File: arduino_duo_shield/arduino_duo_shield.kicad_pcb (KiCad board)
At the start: 2 copper layers, 102.1 x 119.4 mm, 76 parts, among them J2 EStop, J3 Motor_Control, J4 Limit_Switches, J5 inverter_freq, J6 inverter_cmd, J8 inverter_power, J9 Motor_Control_Mirror, K2 JQC-3F, K3 JQC-3F, P10 Digital, P11 PWM, P12 PWM, P13 Communication, P7 Power, P8 Analog, P9 Analog, Q3 2N7000, Q4 BS250, Q5 2N7000, Q6 2N7000, SW1 SW_Push, U1 4504, U2 4504, U3 LM358, U4 74HC14, U6 74HC14, U7 PC817, U8 PC817, U9 PC817

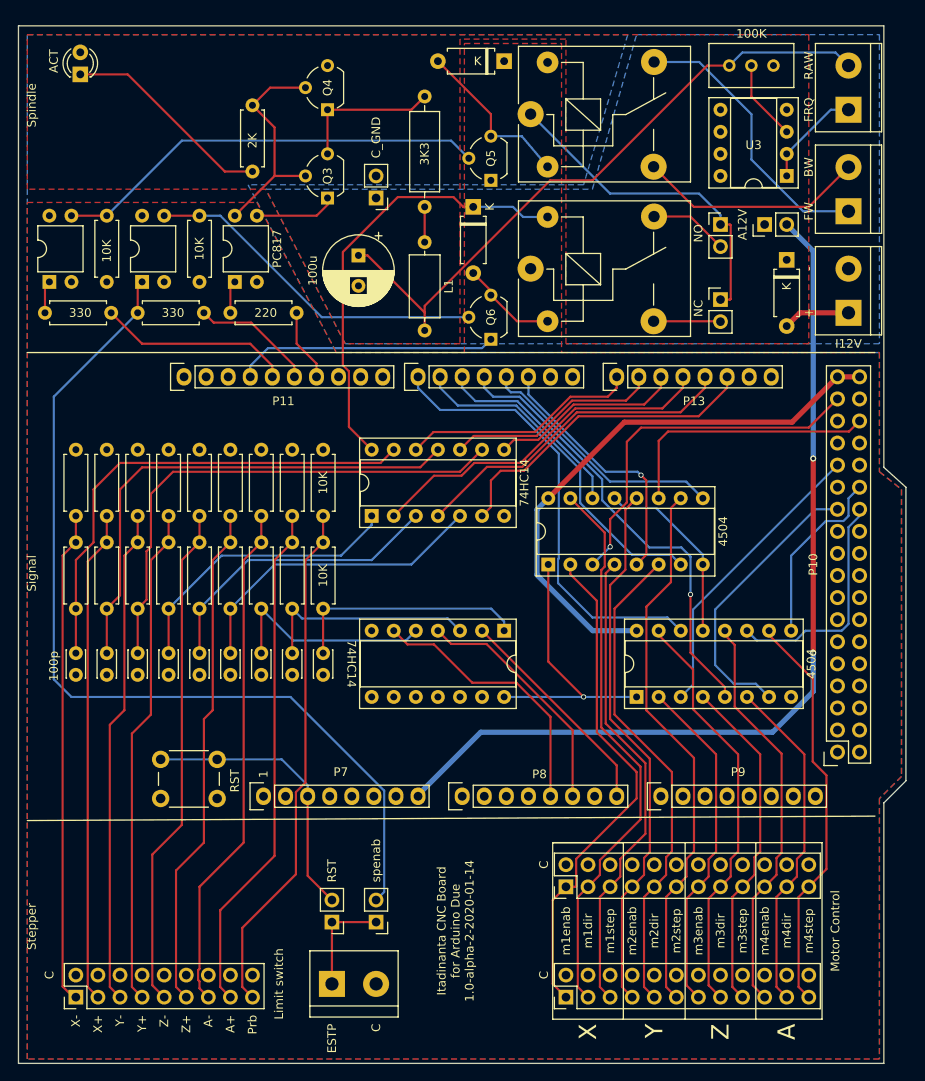
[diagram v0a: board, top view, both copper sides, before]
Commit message: Added screw connectors to everything
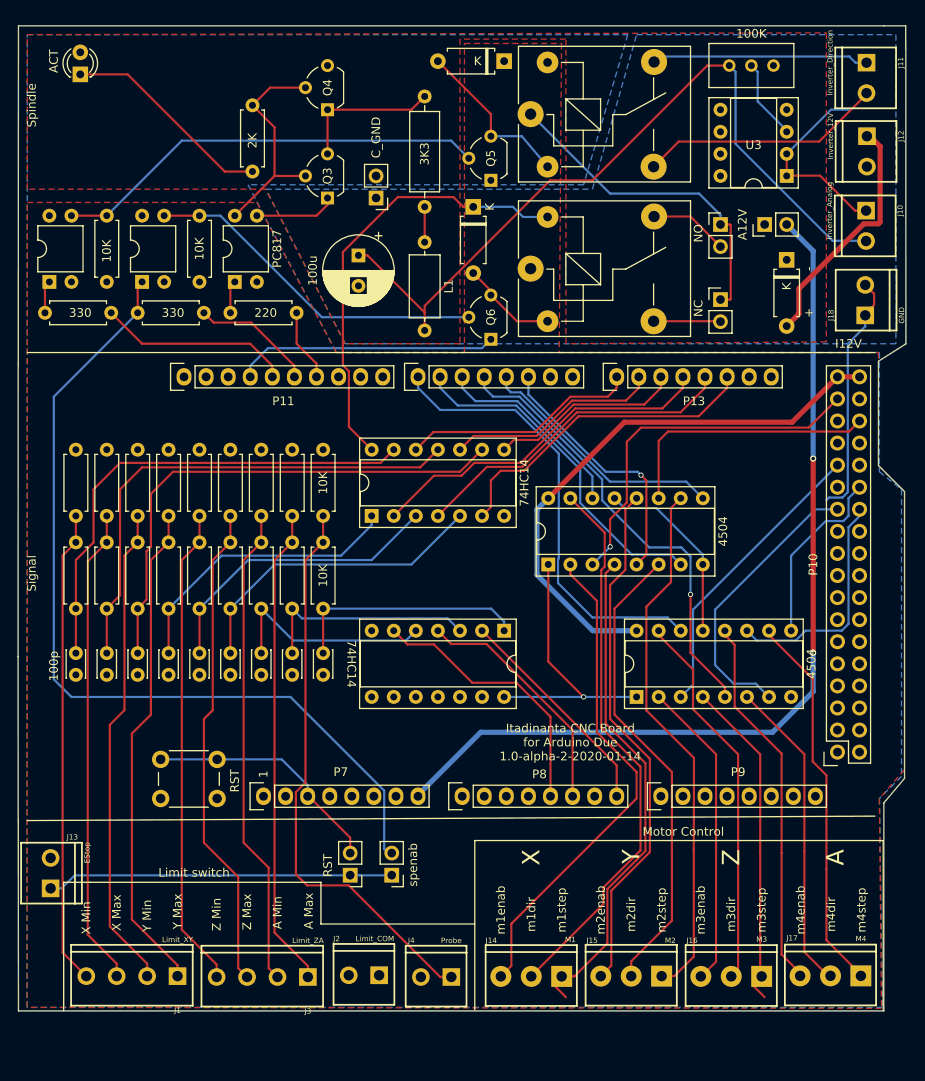
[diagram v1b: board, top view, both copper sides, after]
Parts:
- removed J5: inverter_freq, TerminalBlock:TerminalBlock_bornier-2_P5.08mm
- removed J6: inverter_cmd, TerminalBlock:TerminalBlock_bornier-2_P5.08mm
- removed J8: inverter_power, TerminalBlock:TerminalBlock_bornier-2_P5.08mm
- removed J9: Motor_Control_Mirror, Connector_PinHeader_2.54mm:PinHeader_2x12_P2.54mm_Vertical
- added J1: Limit_XY, Connectors:SCREWTERMINAL-3.5MM-4, F.Cu at (121.4, 139.8)
- added J10: Inverter_Analog, Connectors:SCREWTERMINAL-3.5MM-2, F.Cu at (200.6, 51.7)
- added J11: Inverter_Direction, Connectors:SCREWTERMINAL-3.5MM-2, F.Cu at (200.7, 34.7)
- added J12: Inverter_12V, Connectors:SCREWTERMINAL-3.5MM-2, F.Cu at (200.7, 43.2)
- added J13: EStop, Connectors:SCREWTERMINAL-3.5MM-2, F.Cu at (106.8, 129.7)
- added J14: M1, Connectors:SCREWTERMINAL-3.5MM-3, F.Cu at (165.6, 139.8)
- added J15: M2, Connectors:SCREWTERMINAL-3.5MM-3, F.Cu at (177.1, 139.8)
- added J16: M3, Connectors:SCREWTERMINAL-3.5MM-3, F.Cu at (188.6, 139.8)
- added J17: M4, Connectors:SCREWTERMINAL-3.5MM-3, F.Cu at (200.1, 139.8)
- added J18: GND, Connectors:SCREWTERMINAL-3.5MM-2, F.Cu at (200.6, 63.8)
- J2: value EStop -> Limit_COM; footprint TerminalBlock:TerminalBlock_bornier-2_P5.08mm -> Connectors:SCREWTERMINAL-3.5MM-2
- J3: value Motor_Control -> Limit_ZA; footprint Connector_PinHeader_2.54mm:PinHeader_2x12_P2.54mm_Vertical -> Connectors:SCREWTERMINAL-3.5MM-4
- J4: value Limit_Switches -> Probe; footprint Connector_PinHeader_2.54mm:PinHeader_2x09_P2.54mm_Vertical -> Connectors:SCREWTERMINAL-3.5MM-2
- moved J4 43.3 mm to (152.9, 139.9), turned to 180 degrees
- moved J3 31.5 mm to (136.4, 139.9), turned to 180 degrees
- moved JP5 5.79 mm to (141.3, 128.2)
- moved JP6 5.69 mm to (146.1, 128.2)
- moved J2 5.52 mm to (144.6, 139.7), turned to 180 degrees
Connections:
- J2 pad 1: Net-(J2-Pad1) -> GND
- J3 pad 1: /Level_Shifter/hi_1_1 -> /Debounce_x6/SWAmax+
- J3 pad 2: GND -> /Debounce_x6/SWAmin+
- J3 pad 3: /Level_Shifter/hi_1_2 -> /Debounce_x6/SWZmax+
- J3 pad 4: GND -> /Debounce_x6/SWZmin+
- J4 pad 1: /Debounce_x6/SWXmin+ -> /Debounce_x6/SWProbe+
- JP5 pad 1: Net-(J2-Pad1) -> Net-(J13-Pad1)
- JP6 pad 1: Net-(J2-Pad1) -> Net-(J13-Pad1)
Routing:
- net Net-(J13-Pad1): track 0.00 -> 40.0 mm
- net GND: track 51.8 -> 80.7 mm
- net /Spindle_VFD_Control/inverter_12V: track 7.74 -> 28.0 mm
- net /Spindle_VFD_Control/inverter_frequency_raw_10V: track 74.6 -> 88.8 mm
- net Net-(J2-Pad1): track 12.2 -> 0.00 mm
- net /Spindle_VFD_Control/inverter_frequency_10V: track 11.8 -> 22.4 mm
- net /Spindle_VFD_Control/inverter_fw_switch: track 32.6 -> 26.2 mm
- net /Debounce_x6/SWProbe+: track 59.7 -> 65.3 mm
- net /Spindle_VFD_Control/ext_estop: track 106.2 -> 101.2 mm
- net /Reset: track 32.5 -> 28.1 mm
- net /Level_Shifter/hi_2_2: track 47.9 -> 43.9 mm
- net /Debounce_x6/SWAmax+: track 59.3 -> 55.5 mm
- net /Level_Shifter/hi_2_1: track 39.3 -> 35.7 mm
- net /Level_Shifter/hi_2_4: track 46.8 -> 43.3 mm
- net /Debounce_x6/SWAmin+: track 58.9 -> 55.5 mm
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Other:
- board size 102.1 x 119.4 mm -> 102.2 x 113.3 mm
- board text added: "A Max"
- board text added: "A Min"
- board text added: "X Max"
- board text added: "X Min"
- board text added: "Y Max"
- board text added: "Y Min"
- board text added: "Z Max"
- board text added: "Z Min"
- board text removed: "A+"
- board text removed: "A-"
- board text removed: "BW"
- board text removed: "C"
- board text removed: "ESTP"
- board text removed: "FRQ"
- board text removed: "FW"
- board text removed: "Prb"
- board text removed: "RAW"
- board text removed: "Stepper"
- board text removed: "X+"
- board text removed: "X-"
- board text removed: "Y+"
- board text removed: "Y-"
- board text removed: "Z+"
- board text removed: "Z-"
